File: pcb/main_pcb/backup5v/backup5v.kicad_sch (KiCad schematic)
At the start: 29 parts

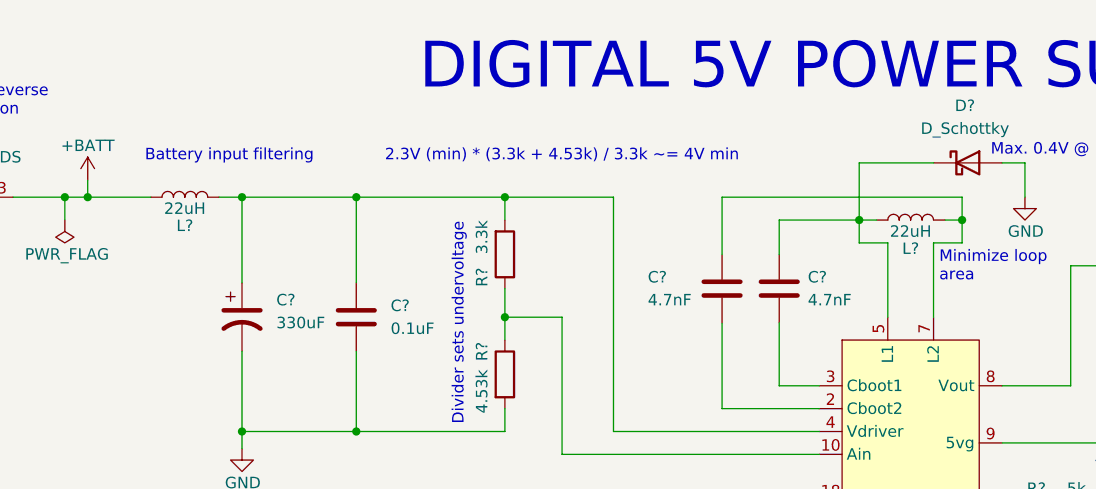
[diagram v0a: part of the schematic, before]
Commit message: fixing errors on PCB as well as readjustments to outline of PCB
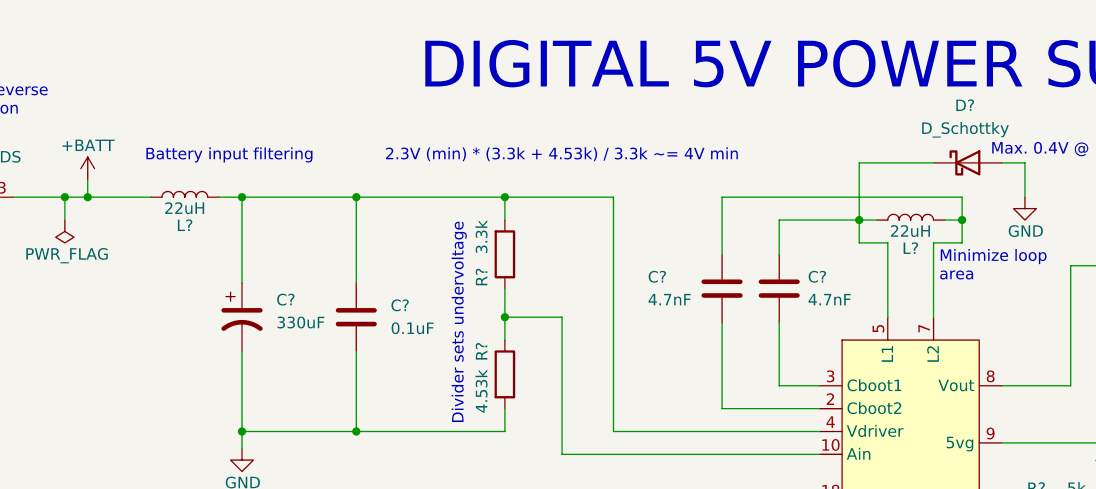
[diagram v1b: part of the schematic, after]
